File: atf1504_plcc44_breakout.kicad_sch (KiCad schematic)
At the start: 9 parts, among them J1 Atmel-JTAG-10, J2 Conn_01x17, J3 Conn_01x17, U1 ATF1504AS-xJx44

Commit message: Update
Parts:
- C1: symbol Device:C_Polarized_Small -> Device:C_Small
- J2, J3: value Conn_01x17 -> Conn_01x18
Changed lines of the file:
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@@
       (effects (font (size 1.27 1.27)) (justify left))
     )
-    (property "Value" "Conn_01x17" (id 1) (at 238.76 64.7699 0)
+    (property "Value" "Conn_01x18" (id 1) (at 238.76 64.7699 0)
       (effects (font (size 1.27 1.27)) (justify left))
     )
@@
     (pin "1")
   )
-  (symbol (lib_id "Device:C_Polarized_Small") (at 74.93 52.07 0) (unit 1)
+  (symbol (lib_id "Device:C_Small") (at 74.93 52.07 0) (unit 1)
     (in_bom yes) (on_board yes) (fields_autoplaced)
     (property "Reference" "C1" (id 0) (at 77.47 50.2538 0)
@@
   (symbol (lib_id "Connector_Generic:Conn_01x18") (at 236.22 114.3 0) (unit 1)
     (in_bom yes) (on_board yes) (fields_autoplaced)
-    (property "Reference" "J2" (id 0) (at 238.76 113.0299 0)
-      (effects (font (size 1.27 1.27)) (justify left))
-    )
-    (property "Value" "Conn_01x17" (id 1) (at 238.76 115.5699 0)
+    (property "Reference" "J2" (id 0) (at 238.76 114.2999 0)
+      (effects (font (size 1.27 1.27)) (justify left))
+    )
+    (property "Value" "Conn_01x18" (id 1) (at 238.76 116.8399 0)
       (effects (font (size 1.27 1.27)) (justify left))
     )
@@
     )
     (path "/c1387fbf-4ab0-4b2a-a08b-0527ff019ac4"
-      (reference "J2") (unit 1) (value "Conn_01x17") (footprint "Connector_PinHeader_2.54mm:PinHeader_1x18_P2.54mm_Vertical")
+      (reference "J2") (unit 1) (value "Conn_01x18") (footprint "Connector_PinHeader_2.54mm:PinHeader_1x18_P2.54mm_Vertical")
     )
     (path "/1e3ef309-85eb-414e-abf6-84fc3d217742"
-      (reference "J3") (unit 1) (value "Conn_01x17") (footprint "Connector_PinHeader_2.54mm:PinHeader_1x18_P2.54mm_Vertical")
+      (reference "J3") (unit 1) (value "Conn_01x18") (footprint "Connector_PinHeader_2.54mm:PinHeader_1x18_P2.54mm_Vertical")
     )
     (path "/33a3fa21-7d1d-4381-98b8-9147b6655499"

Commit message: Update
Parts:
- removed C1: 10u, Capacitor_SMD:C_0805_2012Metric_Pad1.18x1.45mm_HandSolder, symbol Device:C_Small
- added C1: 10u, Capacitor_THT:CP_Radial_D4.0mm_P1.50mm, symbol Device:C_Polarized_Small
- added C6: 100n, Capacitor_SMD:C_0805_2012Metric_Pad1.18x1.45mm_HandSolder, symbol Device:C_Small
- added X1: xMHz, Oscillator:Oscillator_SMD_IQD_IQXO70-4Pin_7.5x5.0mm_HandSoldering, symbol Oscillator:CFPS-72
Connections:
- net GND: now also C1.2, C6.1, X1.2 (GND)
- net I/GCLK1: now also X1.3 (Output)
- net VCC: now also C1.1, C6.2, X1.1 (EN), X1.4 (+Vs)
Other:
- note added: "Optional footprint for SMD clock oscillator connected to GCLK1"

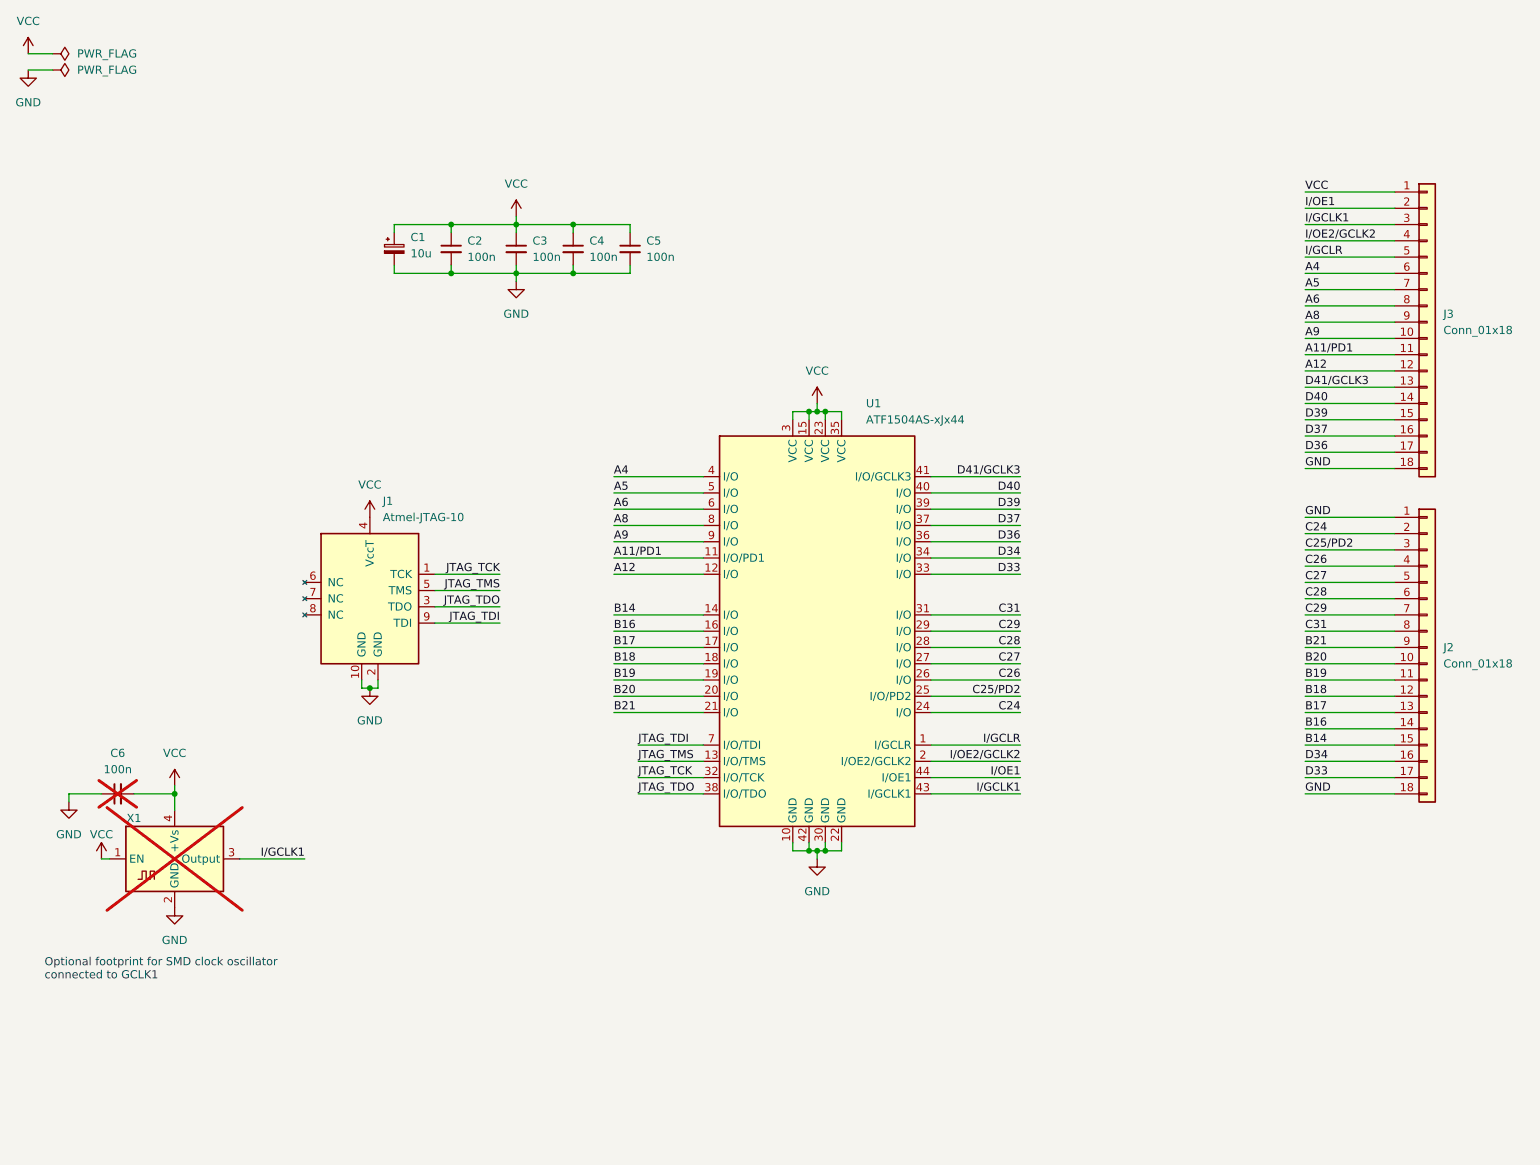
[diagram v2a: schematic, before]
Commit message: Revert oscillator addition
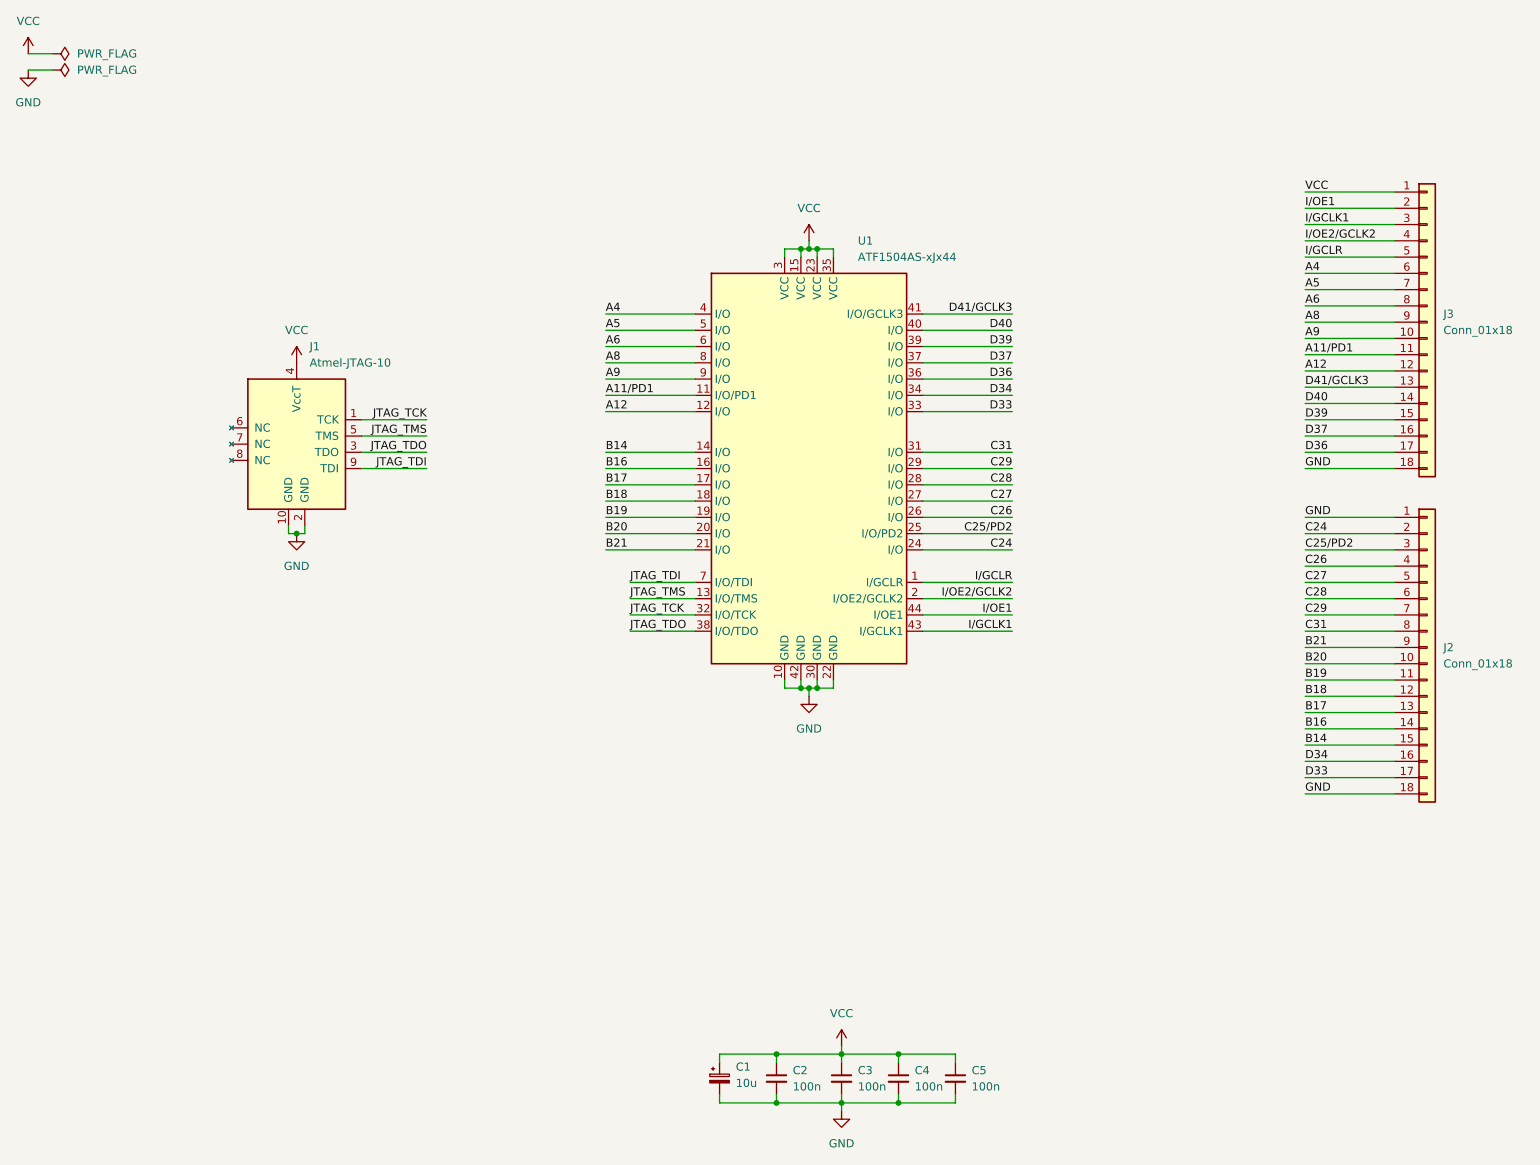
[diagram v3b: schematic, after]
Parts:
- removed C6: 100n, Capacitor_SMD:C_0805_2012Metric_Pad1.18x1.45mm_HandSolder, symbol Device:C_Small
- removed X1: xMHz, Oscillator:Oscillator_SMD_IQD_IQXO70-4Pin_7.5x5.0mm_HandSoldering, symbol Oscillator:CFPS-72
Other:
- note removed: "Optional footprint for SMD clock oscillator connected to GCLK1"
- moved on the sheet: C1, C2, C3, C4, C5, J1, U1

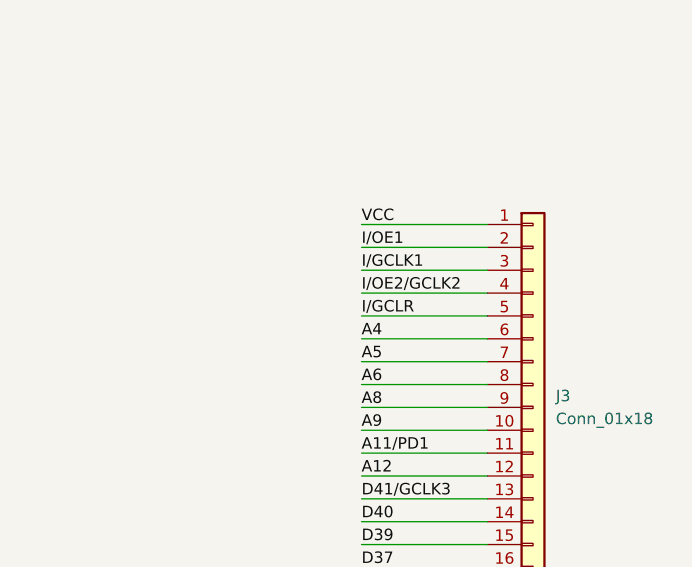
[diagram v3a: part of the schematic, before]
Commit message: Add pin numbers for global inputs and re-order them
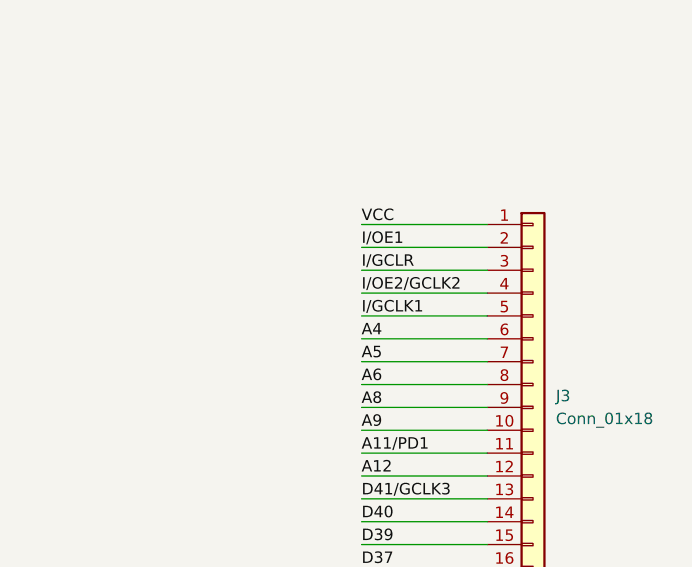
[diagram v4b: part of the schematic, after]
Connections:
- net I/GCLK1: now also J3.5 (Pin_5); no longer J3.3 (Pin_3)
- net I/GCLR: now also J3.3 (Pin_3); no longer J3.5 (Pin_5)
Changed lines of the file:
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@@
   (title_block
     (title "ATF1504 PLCC44 Breakout")
-    (date "2023-06-17")
-    (rev "A")
+    (date "2023-07-15")
+    (rev "B")
     (comment 2 "https://github.com/adrienkohlbecker/atf1504_plcc44_breakout")
     (comment 3 "Licensed under CERN-OHL-W v2")
@@
     (effects (font (size 1.27 1.27)) (justify left bottom))
   )
-  (label "I{slash}GCLR" (at 217.17 53.34 0) (fields_autoplaced)
+  (label "I{slash}GCLR" (at 217.17 48.26 0) (fields_autoplaced)
     (effects (font (size 1.27 1.27)) (justify left bottom))
   )
@@
     (effects (font (size 1.27 1.27)) (justify left bottom))
   )
-  (label "I{slash}GCLK1" (at 217.17 48.26 0) (fields_autoplaced)
-    (effects (font (size 1.27 1.27)) (justify left bottom))
-  )
+  (label "I{slash}GCLK1" (at 217.17 53.34 0) (fields_autoplaced)
+    (effects (font (size 1.27 1.27)) (justify left bottom))
+  )
